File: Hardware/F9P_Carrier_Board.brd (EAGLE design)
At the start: 56.9 x 66 mm, 166 parts, among them J4 U.FL, J5 QWIIC_RIGHT_ANGLE, J6 MICROMOD-2222-C, J8 JTAG, U1 U-BLOX_ZED-F9P, U5 AP7361C-33

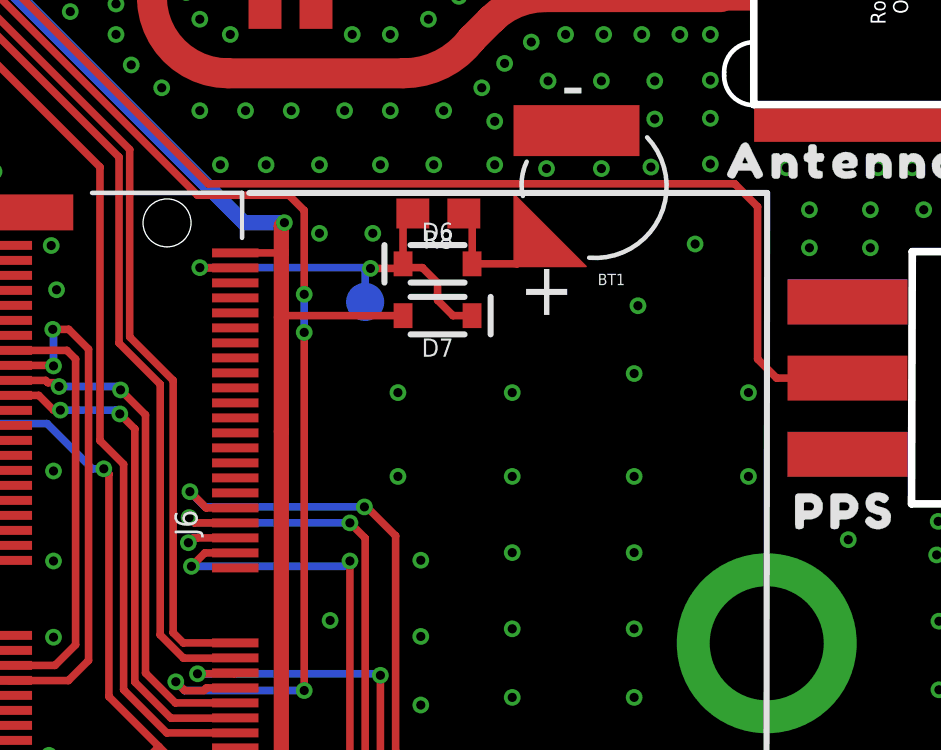
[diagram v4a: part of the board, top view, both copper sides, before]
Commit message: Adds I2C address to schematic, swaps SMA connector to female version
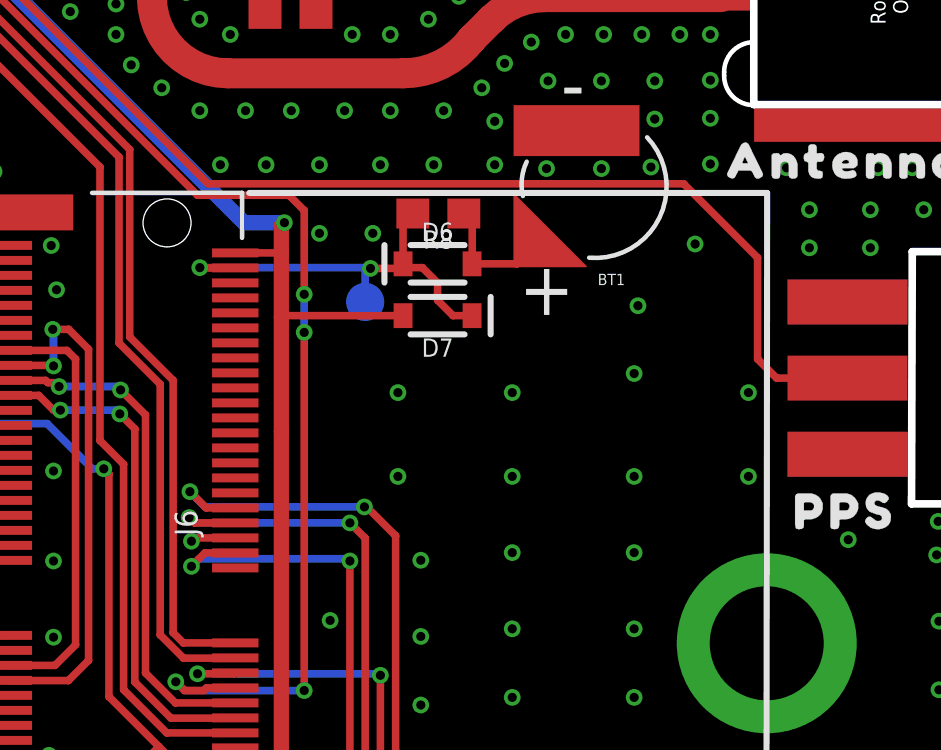
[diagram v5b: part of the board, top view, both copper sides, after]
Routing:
- net PPS: track 100.0 -> 99.0 mm
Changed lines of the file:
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@@
 <setting verticaltext="up"/>
 </settings>
-<grid distance="0.05" unitdist="inch" unit="inch" style="dots" multiple="1" display="yes" altdistance="0.005" altunitdist="inch" altunit="inch"/>
+<grid distance="0.01" unitdist="inch" unit="inch" style="dots" multiple="1" display="yes" altdistance="0.001" altunitdist="inch" altunit="inch"/>
 <layers>
 <layer number="1" name="Top" color="4" fill="1" visible="yes" active="yes"/>
@@
 <element name="J4" library="SparkFun-RF" package="SMA-EDGE-SMD" value="U.FL" x="56.7944" y="33.02" smashed="yes" rot="R270">
 <attribute name="NAME" x="59.3344" y="34.29" size="0.6096" layer="25" font="vector" ratio="20" rot="R270"/>
-<attribute name="PROD_ID" value="CONN-15101" x="56.7944" y="33.02" size="1.778" layer="27" rot="R270" display="off"/>
+<attribute name="PROD_ID" value="CONN-15100" x="56.7944" y="33.02" size="1.778" layer="27" rot="R270" display="off"/>
 </element>
 <element name="C8" library="SparkFun-Capacitors" package="0603" value="47pF" x="34.3408" y="32.4612" smashed="yes">
@@
 <via x="7.5692" y="54.8894" extent="1-16" drill="0.3048"/>
 <via x="26.4414" y="17.224" extent="1-16" drill="0.3048"/>
-<via x="30.9372" y="14.8336" extent="1-16" drill="0.3048"/>
+<via x="31.0388" y="14.8844" extent="1-16" drill="0.3048"/>
 <via x="44.2722" y="50.5714" extent="1-16" drill="0.3048"/>
 <via x="27.2542" y="51.3334" extent="1-16" drill="0.3048"/>
@@
 <contactref element="J7" pad="1"/>
 <wire x1="32.501" y1="14.994" x2="31.206425" y2="14.994" width="0.254" layer="1"/>
-<wire x1="31.206425" y1="14.994" x2="31.198425" y2="14.986" width="0.254" layer="1"/>
-<wire x1="31.198425" y1="14.986" x2="31.0896" y2="14.986" width="0.254" layer="1"/>
-<wire x1="31.0896" y1="14.986" x2="30.9372" y2="14.8336" width="0.254" layer="1"/>
+<wire x1="31.206425" y1="14.994" x2="31.096825" y2="14.8844" width="0.254" layer="1"/>
+<wire x1="31.0388" y1="14.8844" x2="31.096825" y2="14.8844" width="0.254" layer="1"/>
 <via x="47.8282" y="24.7904" extent="1-16" drill="0.3048"/>
 </signal>
@@
 <wire x1="23.1902" y1="39.116" x2="23.1902" y2="35.2044" width="0.254" layer="1"/>
 <wire x1="23.1902" y1="35.2044" x2="31.5976" y2="26.797" width="0.254" layer="1"/>
-<wire x1="49.149" y1="26.797" x2="49.911" y2="26.035" width="0.254" layer="1"/>
-<wire x1="49.911" y1="26.035" x2="49.911" y2="20.955" width="0.254" layer="1"/>
-<wire x1="31.5976" y1="26.797" x2="49.149" y2="26.797" width="0.254" layer="1"/>
+<wire x1="47.4472" y1="26.797" x2="49.911" y2="24.3332" width="0.254" layer="1"/>
+<wire x1="49.911" y1="24.3332" x2="49.911" y2="20.955" width="0.254" layer="1"/>
+<wire x1="31.5976" y1="26.797" x2="47.4472" y2="26.797" width="0.254" layer="1"/>
 <wire x1="49.911" y1="20.955" x2="50.546" y2="20.32" width="0.254" layer="1"/>
 <wire x1="50.546" y1="20.32" x2="52.9082" y2="20.32" width="0.254" layer="1"/>
@@
 <via x="36.322" y="14.224" extent="1-16" drill="0.3048"/>
 <wire x1="36.322" y1="7.2136" x2="36.322" y2="14.224" width="0.254" layer="1"/>
-<wire x1="36.1442" y1="14.0462" x2="36.322" y2="14.224" width="0.254" layer="16"/>
-<wire x1="36.1442" y1="14.0462" x2="31.0388" y2="14.0462" width="0.254" layer="16"/>
+<wire x1="36.322" y1="14.224" x2="36.2458" y2="14.3002" width="0.254" layer="16"/>
+<wire x1="36.2458" y1="14.3002" x2="31.2928" y2="14.3002" width="0.254" layer="16"/>
+<wire x1="31.2928" y1="14.3002" x2="31.0388" y2="14.0462" width="0.254" layer="16"/>
 <contactref element="J7" pad="2"/>
 <wire x1="38.1" y1="1.524" x2="38.1" y2="5.4356" width="0.254" layer="1"/>

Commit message: Removes GPS silk, adds GNSS silk, repanelizes with new silk
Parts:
- U$45: device top:GPS19 -> top:GNSS21
- moved U$45 1.28 mm to (35.6, 27.9)
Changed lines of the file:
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@@
 <setting verticaltext="up"/>
 </settings>
-<grid distance="0.01" unitdist="inch" unit="inch" style="dots" multiple="1" display="yes" altdistance="0.001" altunitdist="inch" altunit="inch"/>
+<grid distance="0.05" unitdist="inch" unit="inch" style="dots" multiple="1" display="yes" altdistance="0.005" altunitdist="inch" altunit="inch"/>
 <layers>
 <layer number="1" name="Top" color="4" fill="1" visible="yes" active="yes"/>
@@
 <element name="U$40" library="bot" package="#RXI2#10" value="" x="44.577" y="61.468" smashed="yes" rot="R270"/>
 <element name="U$44" library="top" package="ZED#F9P19" value="" x="21.209" y="28.194" smashed="yes" rot="MR0"/>
-<element name="U$45" library="top" package="GPS19" value="" x="34.29" y="28.067" smashed="yes" rot="MR0"/>
 <element name="U$49" library="top" package="U#CENTER20" value="" x="3.81" y="49.276" smashed="yes"/>
 <element name="U$50" library="SparkFun-Aesthetics" package="QWIIC_5.5MM" value="" x="53.848" y="50.038" smashed="yes"/>
@@
 <element name="U$77" library="top" package="#GND#0" value="" x="48.2854" y="4.2418" smashed="yes" rot="MR90"/>
 <element name="U$78" library="top" package="#GND#0" value="" x="48.2854" y="4.2418" smashed="yes" rot="R270"/>
+<element name="U$45" library="top" package="GNSS21" value="" x="35.56" y="27.94" smashed="yes" rot="MR0"/>
 </elements>
 <signals>

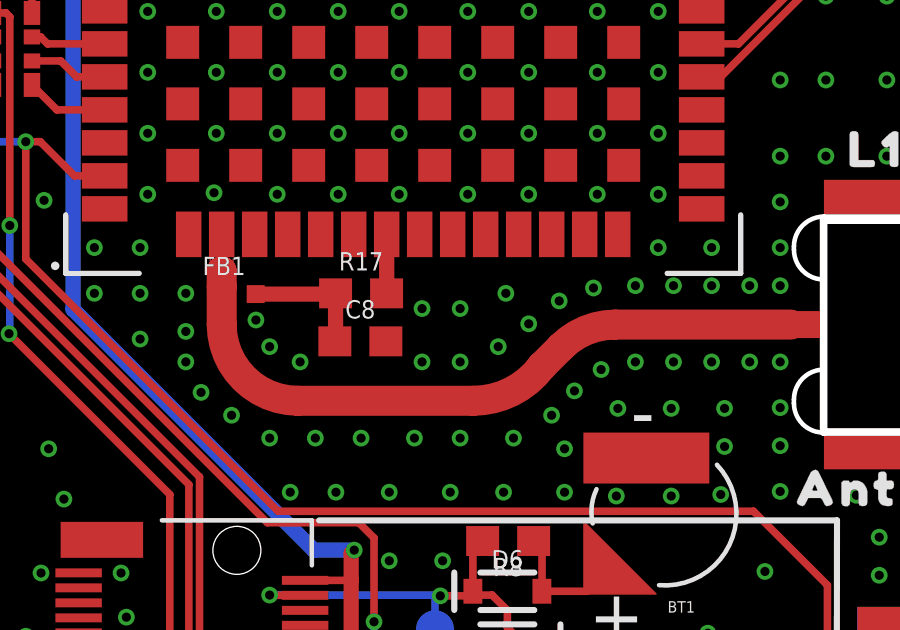
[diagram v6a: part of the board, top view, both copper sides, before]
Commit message: Adds diode protection to antenna
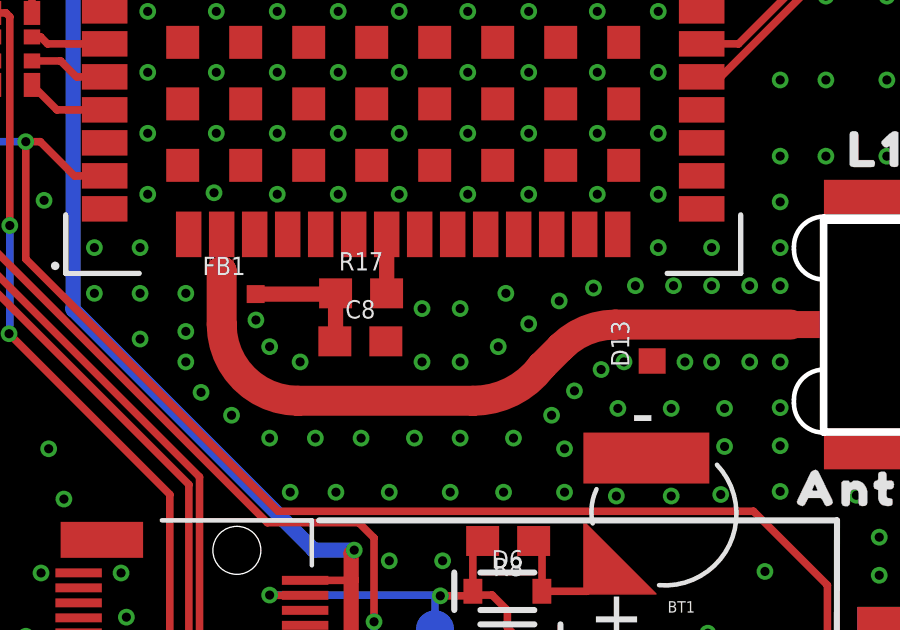
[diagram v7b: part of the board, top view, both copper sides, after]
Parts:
- added D13: PESD0402, SparkFun-DiscreteSemi:0402
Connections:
- net GND: now also D13.1
- net RF_IN: now also D13.2
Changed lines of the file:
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@@
 <layer number="56" name="wert" color="7" fill="1" visible="no" active="no"/>
 <layer number="57" name="tCAD" color="7" fill="1" visible="no" active="no"/>
+<layer number="58" name="bCAD" color="7" fill="1" visible="no" active="no"/>
 <layer number="59" name="tCarbon" color="7" fill="1" visible="no" active="no"/>
 <layer number="60" name="bCarbon" color="7" fill="1" visible="no" active="no"/>
@@
 <layer number="250" name="Descript" color="3" fill="1" visible="no" active="no"/>
 <layer number="251" name="SMDround" color="12" fill="11" visible="no" active="no"/>
+<layer number="253" name="Extra" color="7" fill="1" visible="no" active="no"/>
 <layer number="254" name="cooling" color="7" fill="1" visible="no" active="no"/>
 <layer number="255" name="routoute" color="7" fill="1" visible="no" active="no"/>
@@
 <element name="U$78" library="top" package="#GND#0" value="" x="48.2854" y="4.2418" smashed="yes" rot="R270"/>
 <element name="U$45" library="top" package="GNSS21" value="" x="35.56" y="27.94" smashed="yes" rot="MR0"/>
+<element name="D13" library="SparkFun-DiscreteSemi" package="0402" value="PESD0402" x="44.069" y="32.385" smashed="yes" rot="R90">
+<attribute name="DIGIKEY_PART" value="PESD0402-140CT-ND" x="44.069" y="32.385" size="1.778" layer="27" rot="R90" display="off"/>
+<attribute name="MOUSE_PART" value="650-PESD0402-140" x="44.069" y="32.385" size="1.778" layer="27" rot="R90" display="off"/>
+<attribute name="NAME" x="43.307" y="32.385" size="0.6096" layer="25" font="vector" ratio="20" rot="R90" align="bottom-center"/>
+<attribute name="PROD_ID" value="DIO-15359" x="44.069" y="32.385" size="1.778" layer="27" rot="R90" display="off"/>
+<attribute name="VALUE" x="44.831" y="32.385" size="0.6096" layer="27" font="vector" ratio="20" rot="R90" align="top-center"/>
+</element>
 </elements>
 <signals>
@@
 <via x="40.7162" y="29.9974" extent="1-16" drill="0.3048"/>
 <via x="41.4782" y="30.8102" extent="1-16" drill="0.3048"/>
-<via x="43.5102" y="31.7754" extent="1-16" drill="0.3048"/>
-<via x="44.7802" y="31.7754" extent="1-16" drill="0.3048"/>
+<via x="43.1292" y="31.7754" extent="1-16" drill="0.3048"/>
+<via x="45.1612" y="31.7754" extent="1-16" drill="0.3048"/>
 <via x="46.0502" y="31.7754" extent="1-16" drill="0.3048"/>
 <via x="47.3202" y="31.7754" extent="1-16" drill="0.3048"/>
@@
 <wire x1="31.0388" y1="14.8844" x2="31.096825" y2="14.8844" width="0.254" layer="1"/>
 <via x="47.8282" y="24.7904" extent="1-16" drill="0.3048"/>
+<contactref element="D13" pad="1"/>
 </signal>
 <signal name="3.3V">
@@
 <vertex x="30.099" y="36.195"/>
 </polygon>
-<wire x1="29.72" y1="33.02" x2="29.72" y2="34.29" width="1" layer="1"/>
-<wire x1="29.72" y1="34.798" x2="29.72" y2="34.29" width="1" layer="1"/>
+<wire x1="29.72" y1="33.02" x2="29.72" y2="34.798" width="1" layer="1"/>
 <wire x1="29.72" y1="34.798" x2="29.718" y2="34.798" width="1" layer="1"/>
 <wire x1="32.26" y1="30.48" x2="38.1" y2="30.48" width="1" layer="1"/>
@@
 <wire x1="40.386" y1="31.623" x2="41.03905" y2="32.27605" width="1" layer="1"/>
 <wire x1="41.03905" y1="32.27605" x2="42.835103125" y2="33.02" width="1" layer="1" curve="-45"/>
+<contactref element="D13" pad="2"/>
 <wire x1="42.835103125" y1="33.02" x2="48.6944" y2="33.02" width="1" layer="1"/>
-<wire x1="29.718" y1="34.798" x2="29.853" y2="34.036" width="0" layer="19" extent="1-1"/>
+<wire x1="48.6944" y1="33.02" x2="44.069" y2="32.965" width="0" layer="19" extent="1-1"/>
+<wire x1="29.853" y1="34.036" x2="29.718" y2="34.798" width="0" layer="19" extent="1-1"/>
 </signal>
 <signal name="N$18">

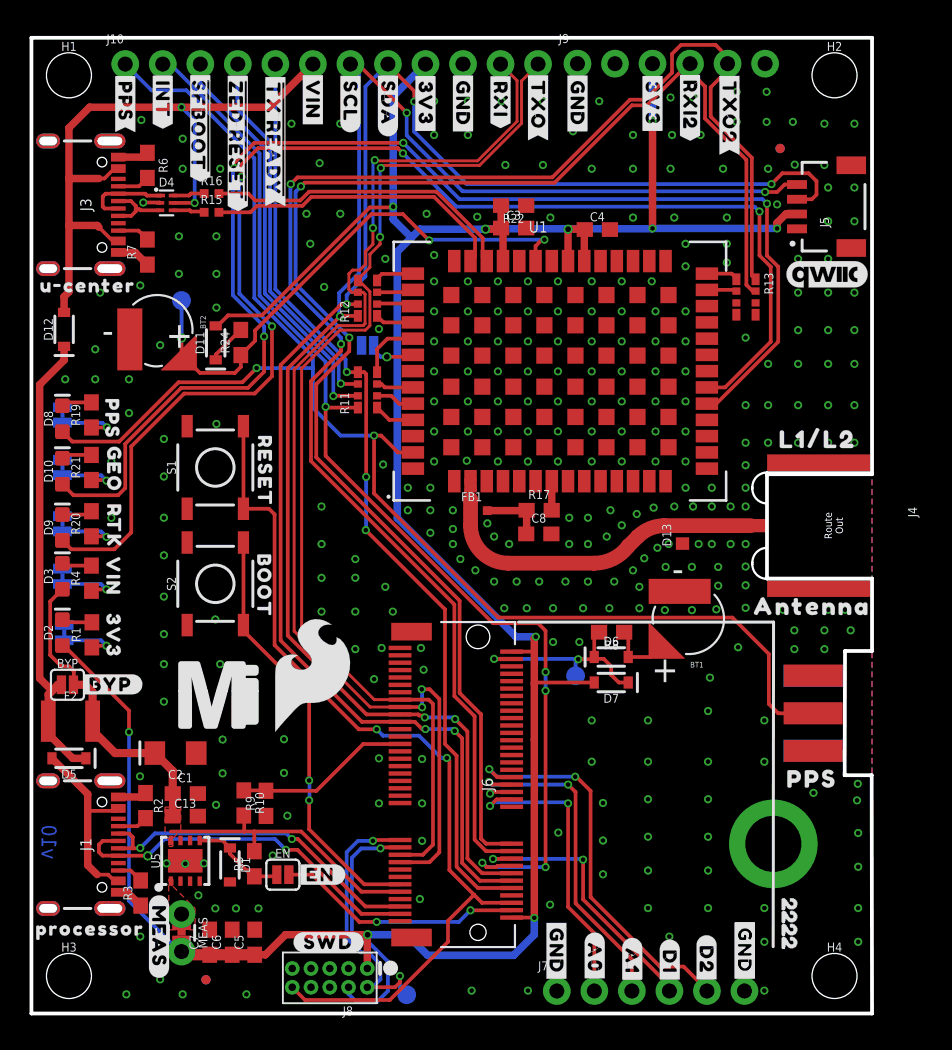
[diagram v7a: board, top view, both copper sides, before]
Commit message: Updates silk, moves 1x6 header to the left .005"
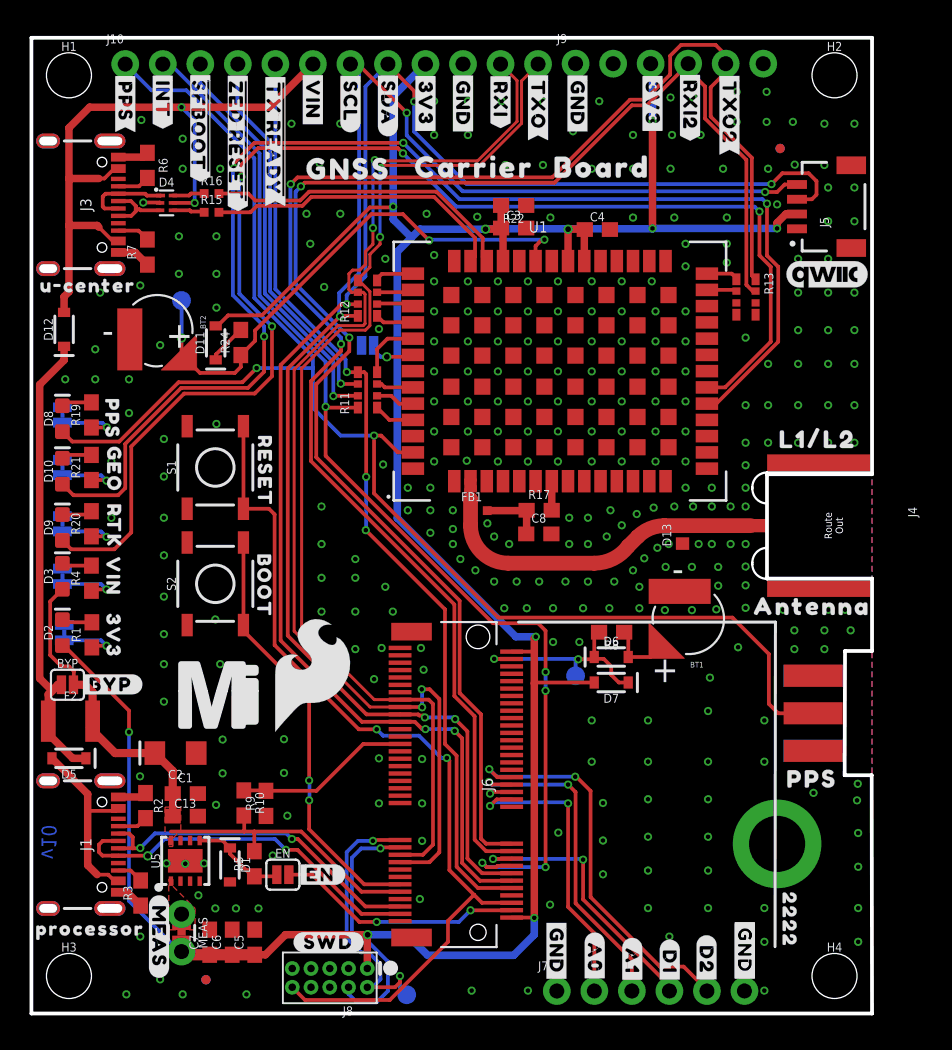
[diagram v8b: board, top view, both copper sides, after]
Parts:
- removed U$55: (no value), buzzard_labels (9):22229
- added U$79: (no value), top:GNSS501
- added U$80: (no value), top:CARRIER502
- added U$81: (no value), top:BOARD503
- added U$82: (no value), top:2222501
- H5: value STAND-OFF-REFLOW2.5MM_TALL -> STAND-OFF-REFLOW-M2.5_2.5MM_TALL
- MEAS: value (none) -> JUMPER-COMBO_2_NC_TRACE
- moved H5 0.25 mm to (50.5, 11.5)
- moved J9 0.13 mm to (36.8, 64.3)
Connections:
- net RTC_3V: now also TP1.1; no longer TP1.P$1
- net SWDIO: now also TP2.1; no longer TP2.P$1
- net V_BATT: now also TP3.1; no longer TP3.P$1
